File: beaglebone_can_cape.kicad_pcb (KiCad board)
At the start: 2 copper layers, 86.4 x 54.6 mm, 32 parts, among them J1 Conn_01x02_Pin, J2 Conn_01x02_Pin, J3 DTM15-12PA, J4 Conn_02x02_Top_Bottom, J5 Battery Harness, P8 BeagleBone_Black_Header, P9 BeagleBone_Black_Header, U1 TCAN332, U2 TCAN332, U3 LMR51430

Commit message: Cleaned up silkscreen layer
* Made all descriptors have the same rotation for cleanliness
* Small bonus, also heavily simplified the battery harness circuit
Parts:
- moved JP3 7.79 mm to (117.2, 85.5), turned to -90 degrees
- moved R6 6.98 mm to (111.5, 85.5), turned to -90 degrees
- moved J5 3.54 mm to (108.1, 90.5), turned to 180 degrees
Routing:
- net Net-(J4-Pin_1): track 23.1 -> 8.64 mm
- net Net-(J4-Pin_3): track 12.2 -> 3.78 mm

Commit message: pushing changes complying with 9.4
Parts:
- moved R3 10.6 mm to (129.5, 78.8), turned to 0 degrees
- moved L1 9.32 mm to (132.8, 75.6), turned to 180 degrees
- moved JP3 7.79 mm to (109.4, 86.5), turned to 0 degrees
- moved R6 6.98 mm to (109.4, 92.2), turned to 0 degrees
- moved Cin1 6.02 mm to (132.2, 91.7), turned to 180 degrees
- moved R4 5.19 mm to (129.5, 85.5), turned to 180 degrees
- moved R5 3.62 mm to (129.5, 81.8), turned to 0 degrees
- moved J5 3.54 mm to (104.6, 90.3), turned to 0 degrees
- moved Cout1 1.14 mm to (122.9, 89.6), turned to -90 degrees
- moved D1 1.08 mm to (136.2, 91.8), turned to 90 degrees
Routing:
- net Net-(J4-Pin_1): track 8.64 -> 23.1 mm
- net +5V: track 21.7 -> 33.5 mm
- net Net-(J4-Pin_3): track 3.78 -> 12.2 mm
- net Net-(U3-SW): track 16.0 -> 8.33 mm
- net +24V: track 36.8 -> 33.3 mm
- net Net-(U3-FB): track 11.1 -> 7.63 mm
- net GND: track 23.9 -> 21.5 mm
- net Net-(R3-Pad2): track 2.45 -> 3.76 mm

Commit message: pushing one more change
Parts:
- moved Cboot1 2.69 mm to (137.7, 78.3), turned to 90 degrees
- moved L1 2.25 mm to (133.8, 77.6), turned to 90 degrees
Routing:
- net Net-(U3-SW): track 8.33 -> 10.3 mm
- net +5V: track 33.5 -> 34.4 mm
- net GND: track 21.5 -> 22.1 mm

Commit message: Revert "pushing one more change"
This reverts commit ff178eb84cf028675ee4f732a8757c322aa0ec1f.
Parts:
- moved Cboot1 2.69 mm to (135.4, 79.7), turned to 180 degrees
- moved L1 2.25 mm to (132.8, 75.6), turned to 180 degrees
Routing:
- net Net-(U3-SW): track 10.3 -> 8.33 mm
- net +5V: track 34.4 -> 33.5 mm
- net GND: track 22.1 -> 21.5 mm

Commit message: Revert "pushing changes complying with 9.4"
This reverts commit c8ddab446e25520ae04b9c74253210672d119c98.
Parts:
- moved R3 10.6 mm to (127.8, 89.2), turned to 90 degrees
- moved L1 9.32 mm to (123.8, 78.1), turned to -90 degrees
- moved JP3 7.79 mm to (117.2, 85.5), turned to -90 degrees
- moved R6 6.98 mm to (111.5, 85.5), turned to -90 degrees
- moved Cin1 6.02 mm to (131.5, 85.8), turned to 90 degrees
- moved R4 5.19 mm to (127.8, 80.6), turned to 90 degrees
- moved R5 3.62 mm to (127.8, 85.0), turned to 90 degrees
- moved J5 3.54 mm to (108.1, 90.5), turned to 180 degrees
- moved Cout1 1.14 mm to (123.6, 90.5), turned to 90 degrees
- moved D1 1.08 mm to (135.2, 91.4), turned to -90 degrees
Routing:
- net Net-(J4-Pin_1): track 23.1 -> 8.64 mm
- net +5V: track 33.5 -> 21.7 mm
- net Net-(J4-Pin_3): track 12.2 -> 3.78 mm
- net Net-(U3-SW): track 8.33 -> 16.0 mm
- net +24V: track 33.3 -> 36.8 mm
- net Net-(U3-FB): track 7.63 -> 11.1 mm
- net GND: track 21.5 -> 23.9 mm
- net Net-(R3-Pad2): track 3.76 -> 2.45 mm

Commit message: updated main with 9.4 changes, with battery stuff etc.
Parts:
- moved L1 11.1 mm to (134.9, 78.6), turned to 90 degrees
- moved R3 9.59 mm to (128.6, 79.7), turned to 0 degrees
- moved R4 7.16 mm to (130.4, 87.2), turned to 180 degrees
- moved Cin1 6.33 mm to (133.0, 91.9), turned to 180 degrees
- moved Cboot1 3.84 mm to (138.0, 82.5), turned to 90 degrees
- moved R5 2.82 mm to (130.4, 84.0), turned to 0 degrees
- moved D1 1.48 mm to (136.6, 92.1), turned to 90 degrees
- moved Cout1 1.16 mm to (123.4, 89.4), turned to -90 degrees
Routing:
- net +5V: track 21.7 -> 33.7 mm
- net Net-(U3-SW): track 16.0 -> 7.36 mm
- net Net-(U3-FB): track 11.1 -> 6.69 mm
- net Net-(U3-CB): track 7.52 -> 3.16 mm
- net GND: track 23.9 -> 19.8 mm
- net +24V: track 36.8 -> 39.2 mm, vias 2 -> 1
- net Net-(R3-Pad2): track 2.45 -> 4.33 mm

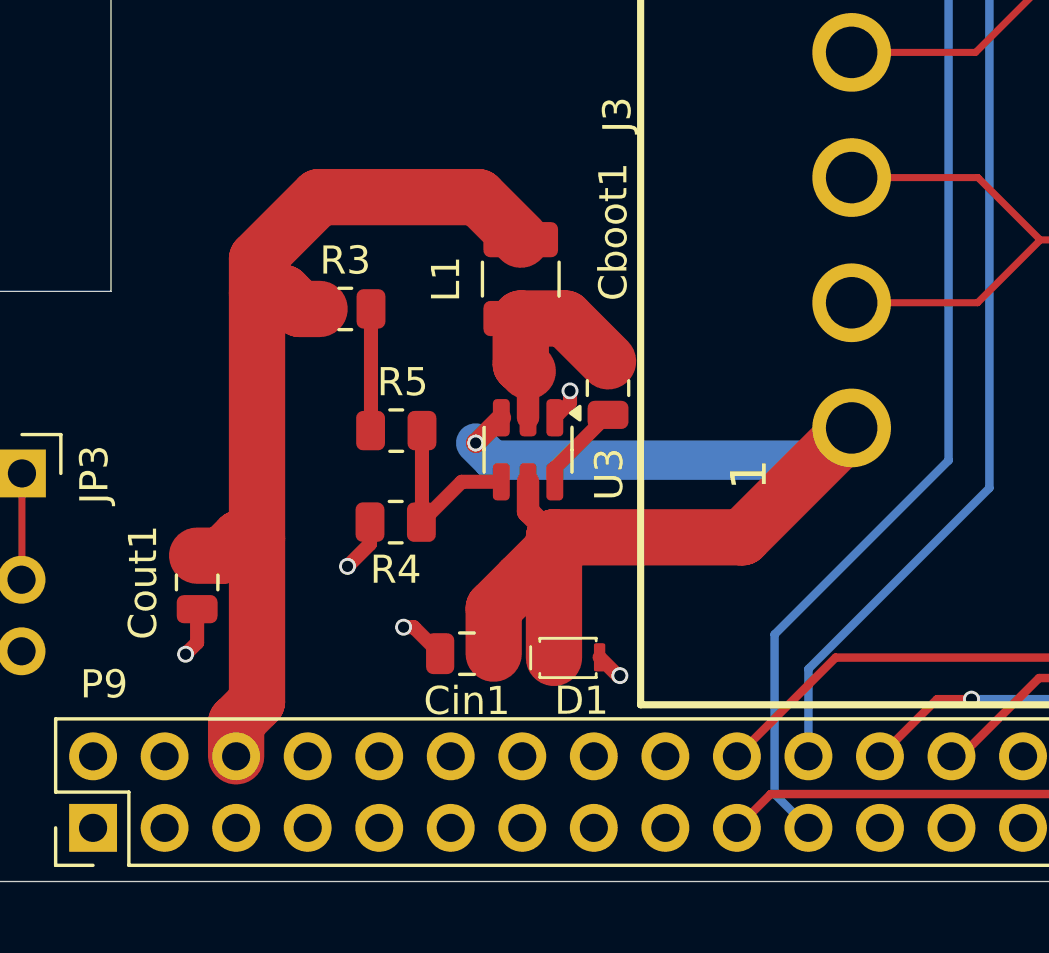
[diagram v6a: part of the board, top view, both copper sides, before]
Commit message: 9.4 Changes
* Checked on the LMR51430 circuit and made R4 + R5 parallel rather than series
* Electrolytic capacitors needed for Cin and Cout
* Rewiring of buck down necessary to fit big boy Caps

Co-Authored-By: Zach Weidner <119375087+WeidnerZ@users.noreply.github.com>
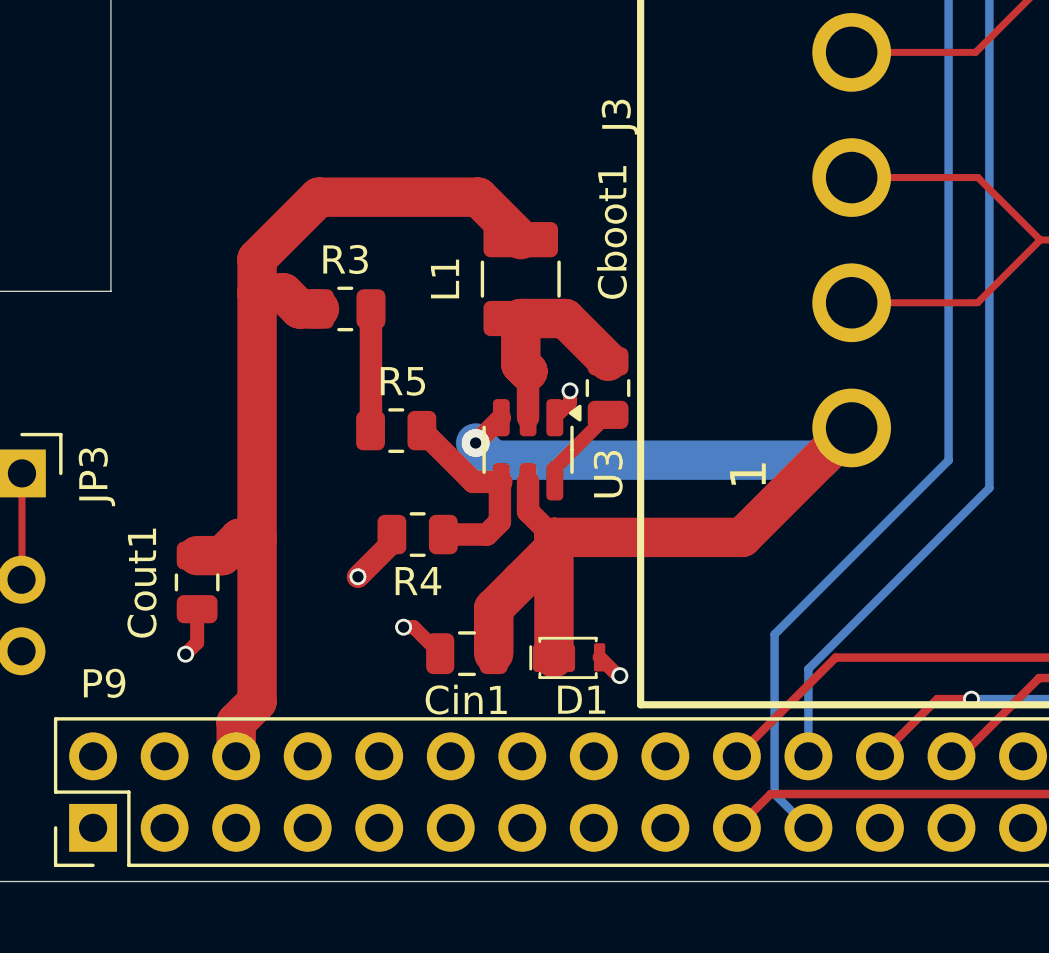
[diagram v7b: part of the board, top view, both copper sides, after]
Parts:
- moved R4 0.90 mm to (131.2, 87.7)
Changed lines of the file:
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@@
 	(footprint "Resistor_SMD:R_0805_2012Metric"
 		(layer "F.Cu")
-		(at 130.43 87.24 180)
+		(at 131.21 87.68 180)
 		(descr "Resistor SMD 0805 (2012 Metric), square (rectangular) end terminal, IPC-7351 nominal, (Body size source: IPC-SM-782 page 72, https://www.pcb-3d.com/wordpress/wp-content/uploads/ipc-sm-782a_amendment_1_and_2.pdf), generated with kicad-footprint-generator")
 		(tags "resistor")
@@
 		(start 127.7 75.7)
 		(end 125.506 77.894)
-		(width 2)
+		(width 1.4)
 		(layer "F.Cu")
 		(net 3)
@@
 		(start 125.506 93.611919)
 		(end 125.506 87.81)
-		(width 2)
+		(width 1.4)
 		(layer "F.Cu")
 		(net 3)
@@
 		(start 134.87 77.21)
 		(end 133.36 75.7)
-		(width 2)
+		(width 1.4)
 		(layer "F.Cu")
 		(net 3)
@@
 		(start 125.506 79.1)
 		(end 126.45 79.1)
-		(width 2)
+		(width 1.4)
 		(layer "F.Cu")
 		(net 3)
@@
 		(start 133.36 75.7)
 		(end 127.7 75.7)
-		(width 2)
+		(width 1.4)
 		(layer "F.Cu")
 		(net 3)
@@
 		(start 125.506 87.81)
 		(end 125.506 79.1)
-		(width 2)
+		(width 1.4)
 		(layer "F.Cu")
 		(net 3)
@@
 		(start 124.89 87.81)
 		(end 124.27 88.43)
-		(width 2)
+		(width 1.4)
 		(layer "F.Cu")
 		(net 3)
@@
 		(start 125.506 79.1)
 		(end 125.506 77.894)
-		(width 2)
+		(width 1.4)
 		(layer "F.Cu")
 		(net 3)
@@
 		(start 124.27 88.43)
 		(end 123.38 88.43)
-		(width 2)
+		(width 1.4)
 		(layer "F.Cu")
 		(net 3)
@@
 		(start 127.02 79.67)
 		(end 127.7275 79.67)
-		(width 2)
+		(width 1.4)
 		(layer "F.Cu")
 		(net 3)
@@
 		(start 125.506 93.611919)
 		(end 124.765 94.352919)
-		(width 2)
+		(width 1.4)
 		(layer "F.Cu")
 		(net 3)
@@
 		(start 125.506 87.81)
 		(end 124.89 87.81)
-		(width 2)
+		(width 1.4)
 		(layer "F.Cu")
 		(net 3)
@@
 		(start 124.765 94.352919)
 		(end 124.765 95.555)
-		(width 2)
+		(width 1.4)
 		(layer "F.Cu")
 		(net 3)
@@
 		(start 126.45 79.1)
 		(end 127.02 79.67)
-		(width 2)
+		(width 1.4)
 		(layer "F.Cu")
 		(net 3)
@@
 	)
 	(segment
+		(start 130.2975 87.68)
+		(end 130.2975 87.9725)
+		(width 0.8)
+		(layer "F.Cu")
+		(net 11)
+	)
+	(segment
 		(start 137.67 92.04)
 		(end 138.32 92.69)
@@
 	)
 	(segment
-		(start 129.5175 88.0125)
-		(end 128.72 88.81)
-		(width 0.5)
-		(layer "F.Cu")
-		(net 11)
-	)
-	(segment
 		(start 179.31 83.34)
 		(end 179.625 83.025)
@@
 	)
 	(segment
+		(start 130.2975 87.9725)
+		(end 129.09 89.18)
+		(width 0.8)
+		(layer "F.Cu")
+		(net 11)
+	)
+	(segment
 		(start 136.62 82.58)
 		(end 136.62 82.56)
@@
 	)
 	(segment
-		(start 129.5175 87.24)
-		(end 129.5175 88.0125)
-		(width 0.5)
-		(layer "F.Cu")
-		(net 11)
-	)
-	(segment
 		(start 169.48 82.87)
 		(end 169.25 83.1)
@@
 	)
 	(via
-		(at 177.42 56.35)
+		(at 129.09 89.18)
 		(size 0.6)
 		(drill 0.4)
@@
 	)
 	(via
-		(at 122.97 91.93)
+		(at 177.42 56.35)
 		(size 0.6)
 		(drill 0.4)
@@
 	)
 	(via
-		(at 138.39 92.69)
+		(at 122.97 91.93)
 		(size 0.6)
 		(drill 0.4)
@@
 	)
 	(via
-		(at 128.72 88.81)
+		(at 138.39 92.69)
 		(size 0.6)
 		(drill 0.4)
@@
 		(start 135.13 81.89)
 		(end 135.12 81.88)
-		(width 0.8)
+		(width 1.4)
 		(layer "F.Cu")
 		(net 12)
@@
 		(start 135.12 81.88)
 		(end 134.87 81.63)
-		(width 2)
+		(width 1.4)
 		(layer "F.Cu")
 		(net 12)
@@
 		(start 137.97 81.53)
 		(end 136.45 80.01)
-		(width 2)
+		(width 1.4)
 		(layer "F.Cu")
 		(net 12)
@@
 		(start 136.45 80.01)
 		(end 134.87 80.01)
-		(width 2)
+		(width 1.4)
 		(layer "F.Cu")
 		(net 12)
@@
 		(start 134.87 81.63)
 		(end 134.87 80.01)
-		(width 2)
+		(width 1.4)
 		(layer "F.Cu")
 		(net 12)
@@
 		(start 134.9 89.31)
 		(end 136.05 88.16)
-		(width 2)
+		(width 1.4)
 		(layer "F.Cu")
 		(net 14)
@@
 		(start 136.05 87.78)
 		(end 142.735 87.78)
-		(width 2)
+		(width 1.4)
 		(layer "F.Cu")
 		(net 14)
@@
 		(start 136.05 87.78)
 		(end 136.05 92.06)
-		(width 2)
+		(width 1.4)
 		(layer "F.Cu")
 		(net 14)
@@
 		(start 142.735 87.78)
 		(end 146.62 83.895)
-		(width 2)
+		(width 1.4)
 		(layer "F.Cu")
 		(net 14)
@@
 		(start 133.91 90.3)
 		(end 134.9 89.31)
-		(width 2)
+		(width 1.4)
 		(layer "F.Cu")
 		(net 14)
@@
 		(start 136.05 88.16)
 		(end 136.05 87.78)
-		(width 2)
+		(width 1.4)
 		(layer "F.Cu")
 		(net 14)
@@
 		(start 133.91 91.91)
 		(end 133.91 90.3)
-		(width 2)
+		(width 1.4)
 		(layer "F.Cu")
 		(net 14)
@@
 	(via
 		(at 133.27 84.43)
-		(size 0.6)
+		(size 1)
 		(drill 0.4)
 		(layers "F.Cu" "B.Cu")
@@
 		(start 129.5525 79.67)
 		(end 129.5525 83.975)
-		(width 0.5)
+		(width 0.8)
 		(layer "F.Cu")
 		(net 15)
 	)
 	(segment
-		(start 134.18 85.8075)
-		(end 132.775 85.8075)
-		(width 0.5)
+		(start 134.129 87.221)
+		(end 134.129 85.8075)
+		(width 0.8)
 		(layer "F.Cu")
 		(net 16)
 	)
 	(segment
-		(start 132.775 85.8075)
-		(end 131.3425 87.24)
-		(width 0.5)
+		(start 133.67 87.68)
+		(end 134.129 87.221)
+		(width 0.8)
 		(layer "F.Cu")
 		(net 16)
 	)
 	(segment
-		(start 131.3625 87.22)
-		(end 131.3425 87.24)
-		(width 0.5)
+		(start 133.18 85.8075)
+		(end 134.18 85.8075)
+		(width 0.8)
 		(layer "F.Cu")
 		(net 16)
@@
 	(segment
 		(start 131.3625 83.99)
-		(end 131.3625 87.22)
-		(width 0.5)
+		(end 133.18 85.8075)
+		(width 0.8)
+		(layer "F.Cu")
+		(net 16)
+	)
+	(segment
+		(start 132.1225 87.68)
+		(end 133.67 87.68)
+		(width 0.8)
 		(layer "F.Cu")
 		(net 16)

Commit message: pushing changes with big caps
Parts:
- Cin1, Cout1: footprint Capacitor_SMD:C_0805_2012Metric -> Capacitor_SMD:CP_Elec_6.3x5.4
- moved Cout1 19.7 mm to (128.3, 70.3), turned to 180 degrees
- moved Cin1 2.73 mm to (131.0, 90.0)
- moved R4 2.56 mm to (130.3, 85.3)
- moved D1 2.05 mm to (138.0, 90.6), turned to 0 degrees
- moved R5 1.71 mm to (130.5, 82.3)
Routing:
- net +5V: track 33.7 -> 39.5 mm
- net GND: track 19.9 -> 23.3 mm
- net +24V: track 39.2 -> 36.8 mm
- net Net-(R3-Pad2): track 4.33 -> 2.63 mm
- net Net-(U3-FB): track 7.18 -> 7.90 mm
